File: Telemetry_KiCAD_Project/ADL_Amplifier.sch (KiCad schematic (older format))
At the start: 7 parts

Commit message: Annotated Components
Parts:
- gave numbers to parts that had none: 7
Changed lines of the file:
@@
 $Descr A4 11693 8268
 encoding utf-8
-Sheet 6 8
+Sheet 4 8
 Title ""
 Date ""
@@
 $EndDescr
 $Comp
-L power:GND #PWR?
+L power:GND #PWR0112
 U 1 1 619F7B7D
 P 4150 3300
-F 0 "#PWR?" H 4150 3050 50  0001 C CNN
+F 0 "#PWR0112" H 4150 3050 50  0001 C CNN
 F 1 "GND" H 4155 3127 50  0000 C CNN
 F 2 "" H 4150 3300 50  0001 C CNN
@@
 $EndComp
 $Comp
-L Device:L_Small L?
+L Device:L_Small L7
 U 1 1 619F8B95
 P 3500 3100
-F 0 "L?" V 3685 3100 50  0000 C CNN
+F 0 "L7" V 3685 3100 50  0000 C CNN
 F 1 "L_Small" V 3594 3100 50  0000 C CNN
 F 2 "" H 3500 3100 50  0001 C CNN
@@
 $EndComp
 $Comp
-L Device:C_Small C?
+L Device:C_Small C9
 U 1 1 619F9969
 P 3200 3250
-F 0 "C?" H 3108 3204 50  0000 R CNN
+F 0 "C9" H 3108 3204 50  0000 R CNN
 F 1 "2.4pF" H 3108 3295 50  0000 R CNN
 F 2 "" H 3200 3250 50  0001 C CNN
@@
 $EndComp
 $Comp
-L power:GND #PWR?
+L power:GND #PWR0113
 U 1 1 619F9C64
 P 3200 3350
-F 0 "#PWR?" H 3200 3100 50  0001 C CNN
+F 0 "#PWR0113" H 3200 3100 50  0001 C CNN
 F 1 "GND" H 3205 3177 50  0000 C CNN
 F 2 "" H 3200 3350 50  0001 C CNN
@@
 Connection ~ 3200 3100
 $Comp
-L RDT_Custom_Symbols:ADL5521 U?
+L RDT_Custom_Symbols:ADL5521 U3
 U 1 1 619FB6E9
 P 3850 2850
-F 0 "U?" H 4150 3015 50  0000 C CNN
+F 0 "U3" H 4150 3015 50  0000 C CNN
 F 1 "ADL5521" H 4150 2924 50  0000 C CNN
 F 2 "Package_CSP:Analog_LFCSP-8-1EP_3x3mm_P0.5mm_EP1.53x1.85mm" H 4150 3100 50  0001 C CNN
@@
 $EndComp
 $Comp
-L Device:R_Small R?
+L Device:R_Small R1
 U 1 1 619FBF87
 P 4150 2600
-F 0 "R?" V 3954 2600 50  0000 C CNN
+F 0 "R1" V 3954 2600 50  0000 C CNN
 F 1 "1.3k" V 4045 2600 50  0000 C CNN
 F 2 "" H 4150 2600 50  0001 C CNN
@@
 Connection ~ 4550 2600
 $Comp
-L Device:L_Small L?
+L Device:L_Small L8
 U 1 1 619FDCB0
 P 4550 2300
-F 0 "L?" H 4700 2250 50  0000 R CNN
+F 0 "L8" H 4700 2250 50  0000 R CNN
 F 1 "3.4nH" H 4900 2350 50  0000 R CNN
 F 2 "" H 4550 2300 50  0001 C CNN
@@
 $EndComp
 $Comp
-L Device:C_Small C?
+L Device:C_Small C10
 U 1 1 619FE8E9
 P 4750 2100
-F 0 "C?" V 4521 2100 50  0000 C CNN
+F 0 "C10" V 4521 2100 50  0000 C CNN
 F 1 "100nF" V 4600 2150 50  0000 C CNN
 F 2 "" H 4750 2100 50  0001 C CNN
@@
 	4550 2100 4650 2100
 $Comp
-L power:GND #PWR?
+L power:GND #PWR0114
 U 1 1 619FF3E9
 P 5000 2200
-F 0 "#PWR?" H 5000 1950 50  0001 C CNN
+F 0 "#PWR0114" H 5000 1950 50  0001 C CNN
 F 1 "GND" H 5005 2027 50  0000 C CNN
 F 2 "" H 5000 2200 50  0001 C CNN
@@
 	5000 2100 4850 2100
 $Comp
-L Device:R_Small R?
+L Device:R_Small R2
 U 1 1 61A005B8
 P 4550 1950
-F 0 "R?" H 4750 1900 50  0000 R CNN
+F 0 "R2" H 4750 1900 50  0000 R CNN
 F 1 "R_Small" H 4950 2000 50  0000 R CNN
 F 2 "" H 4550 1950 50  0001 C CNN
@@
 	4550 2400 4550 2600
 $Comp
-L power:+5V #PWR?
+L power:+5V #PWR0115
 U 1 1 61A03221
 P 4550 1800
-F 0 "#PWR?" H 4550 1650 50  0001 C CNN
+F 0 "#PWR0115" H 4550 1650 50  0001 C CNN
 F 1 "+5V" H 4565 1973 50  0000 C CNN
 F 2 "" H 4550 1800 50  0001 C CNN

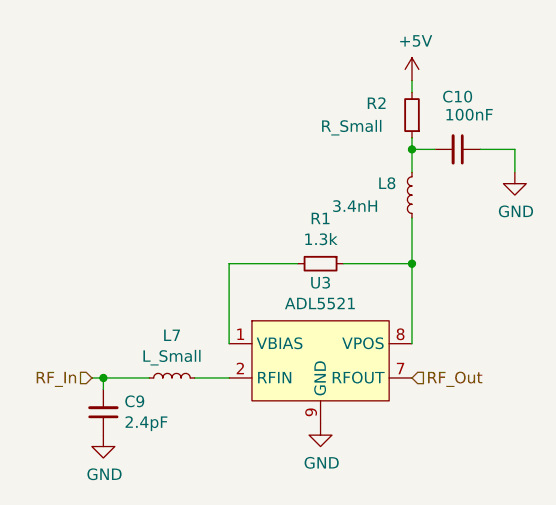
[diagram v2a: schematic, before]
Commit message: Corrected hierarchical pin directions, squashed bugs
There are still some warnings about pins being connected but not driven, don't know how to fix those at the moment
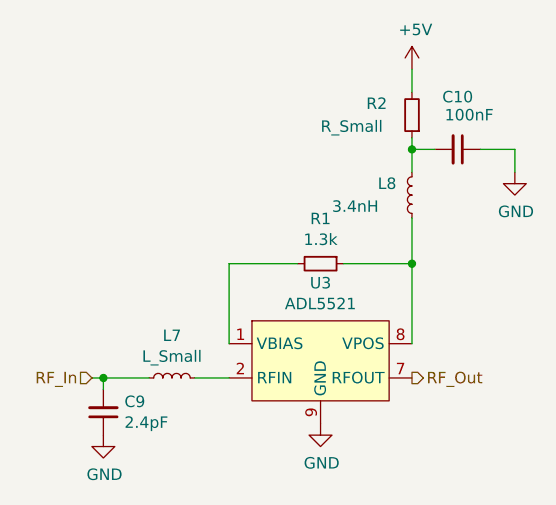
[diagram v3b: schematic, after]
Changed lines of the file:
@@
 Wire Wire Line
 	4550 2600 4550 2950
-Text HLabel 4550 3100 2    50   Input ~ 0
+Text HLabel 4550 3100 2    50   Output ~ 0
 RF_Out
 Connection ~ 4550 2600
@@
 L power:+5V #PWR0115
 U 1 1 61A03221
-P 4550 1800
-F 0 "#PWR0115" H 4550 1650 50  0001 C CNN
-F 1 "+5V" H 4565 1973 50  0000 C CNN
-F 2 "" H 4550 1800 50  0001 C CNN
-F 3 "" H 4550 1800 50  0001 C CNN
-	1    4550 1800
+P 4550 1750
+F 0 "#PWR0115" H 4550 1600 50  0001 C CNN
+F 1 "+5V" H 4565 1923 50  0000 C CNN
+F 2 "" H 4550 1750 50  0001 C CNN
+F 3 "" H 4550 1750 50  0001 C CNN
+	1    4550 1750
 	1    0    0    -1
 $EndComp
 Wire Wire Line
-	4550 1800 4550 1850
+	4550 1750 4550 1850
 $EndSCHEMATC

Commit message: Assigned footprints to all components (except duplexer)
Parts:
- C10, C9: footprint (none) -> Capacitor_SMD:C_0603_1608Metric
- L7, L8: footprint (none) -> Inductor_SMD:L_0603_1608Metric
- R1, R2: footprint (none) -> Resistor_SMD:R_0201_0603Metric
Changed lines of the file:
@@
 F 0 "L7" V 3685 3100 50  0000 C CNN
 F 1 "L_Small" V 3594 3100 50  0000 C CNN
-F 2 "" H 3500 3100 50  0001 C CNN
+F 2 "Inductor_SMD:L_0603_1608Metric" H 3500 3100 50  0001 C CNN
 F 3 "~" H 3500 3100 50  0001 C CNN
 	1    3500 3100
@@
 F 0 "C9" H 3108 3204 50  0000 R CNN
 F 1 "2.4pF" H 3108 3295 50  0000 R CNN
-F 2 "" H 3200 3250 50  0001 C CNN
+F 2 "Capacitor_SMD:C_0603_1608Metric" H 3200 3250 50  0001 C CNN
 F 3 "~" H 3200 3250 50  0001 C CNN
 	1    3200 3250
@@
 F 0 "R1" V 3954 2600 50  0000 C CNN
 F 1 "1.3k" V 4045 2600 50  0000 C CNN
-F 2 "" H 4150 2600 50  0001 C CNN
+F 2 "Resistor_SMD:R_0201_0603Metric" H 4150 2600 50  0001 C CNN
 F 3 "~" H 4150 2600 50  0001 C CNN
 	1    4150 2600
@@
 F 0 "L8" H 4700 2250 50  0000 R CNN
 F 1 "3.4nH" H 4900 2350 50  0000 R CNN
-F 2 "" H 4550 2300 50  0001 C CNN
+F 2 "Inductor_SMD:L_0603_1608Metric" H 4550 2300 50  0001 C CNN
 F 3 "~" H 4550 2300 50  0001 C CNN
 	1    4550 2300
@@
 F 0 "C10" V 4521 2100 50  0000 C CNN
 F 1 "100nF" V 4600 2150 50  0000 C CNN
-F 2 "" H 4750 2100 50  0001 C CNN
+F 2 "Capacitor_SMD:C_0603_1608Metric" H 4750 2100 50  0001 C CNN
 F 3 "~" H 4750 2100 50  0001 C CNN
 	1    4750 2100
@@
 F 0 "R2" H 4750 1900 50  0000 R CNN
 F 1 "R_Small" H 4950 2000 50  0000 R CNN
-F 2 "" H 4550 1950 50  0001 C CNN
+F 2 "Resistor_SMD:R_0201_0603Metric" H 4550 1950 50  0001 C CNN
 F 3 "~" H 4550 1950 50  0001 C CNN
 	1    4550 1950

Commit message: Created separate schematics for chips acting in TX and RX
Added link to document describing passive component selection
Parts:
- U3: footprint Package_CSP:Analog_LFCSP-8-1EP_3x3mm_P0.5mm_EP1.53x1.85mm -> Package_CSP:LFCSP-8-1EP_3x3mm_P0.5mm_EP1.45x1.74mm
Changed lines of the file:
@@
 F 0 "U3" H 4150 3015 50  0000 C CNN
 F 1 "ADL5521" H 4150 2924 50  0000 C CNN
-F 2 "Package_CSP:Analog_LFCSP-8-1EP_3x3mm_P0.5mm_EP1.53x1.85mm" H 4150 3100 50  0001 C CNN
+F 2 "Package_CSP:LFCSP-8-1EP_3x3mm_P0.5mm_EP1.45x1.74mm" H 4150 3100 50  0001 C CNN
 F 3 "https://www.analog.com/media/en/technical-documentation/data-sheets/ADL5521.pdf" H 3850 2850 50  0001 C CNN
 	1    3850 2850

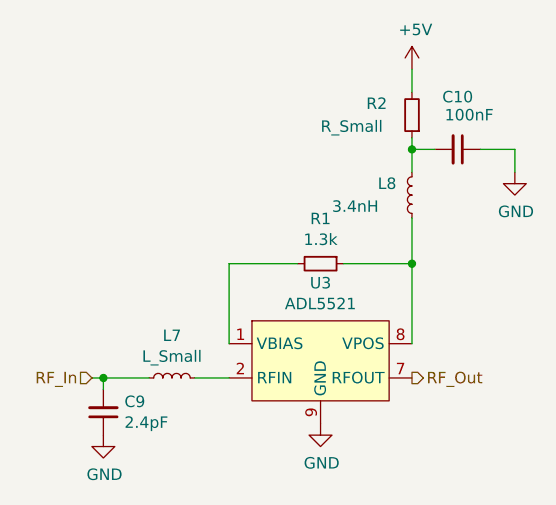
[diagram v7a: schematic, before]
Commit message: Added RSD Duplexer Footprint, rearranged RF matching networks
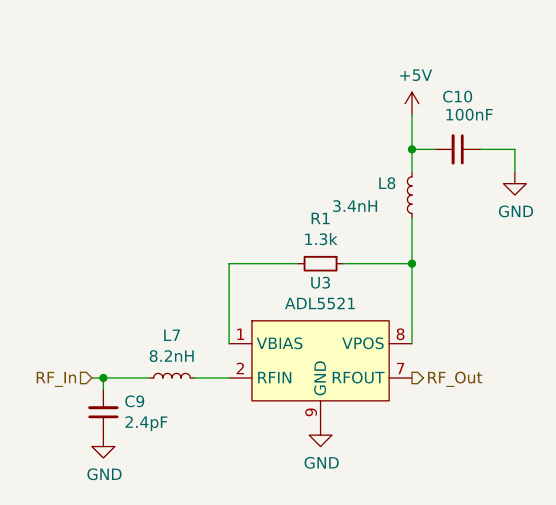
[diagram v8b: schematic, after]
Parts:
- removed R2: R_Small, Resistor_SMD:R_0201_0603Metric, symbol Device:R_Small
- L7: value L_Small -> 8.2nH
- R1: footprint Resistor_SMD:R_0201_0603Metric -> Resistors:0603
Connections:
- net +5V: now also C10.2, L8.2
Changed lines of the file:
@@
-$EndComp
-$Comp
-L Device:L_Small L7
-U 1 1 619F8B95
-P 3500 3100
-F 0 "L7" V 3685 3100 50  0000 C CNN
-F 1 "L_Small" V 3594 3100 50  0000 C CNN
-F 2 "Inductor_SMD:L_0603_1608Metric" H 3500 3100 50  0001 C CNN
-F 3 "~" H 3500 3100 50  0001 C CNN
-	1    3500 3100
-	0    -1   -1   0
 $EndComp
 $Comp
@@
 F 0 "R1" V 3954 2600 50  0000 C CNN
 F 1 "1.3k" V 4045 2600 50  0000 C CNN
-F 2 "Resistor_SMD:R_0201_0603Metric" H 4150 2600 50  0001 C CNN
+F 2 "Resistors:0603" H 4150 2600 50  0001 C CNN
 F 3 "~" H 4150 2600 50  0001 C CNN
 	1    4150 2600
@@
 Wire Wire Line
 	5000 2100 4850 2100
-$Comp
-L Device:R_Small R2
-U 1 1 61A005B8
-P 4550 1950
-F 0 "R2" H 4750 1900 50  0000 R CNN
-F 1 "R_Small" H 4950 2000 50  0000 R CNN
-F 2 "Resistor_SMD:R_0201_0603Metric" H 4550 1950 50  0001 C CNN
-F 3 "~" H 4550 1950 50  0001 C CNN
-	1    4550 1950
-	-1   0    0    1
-$EndComp
-Wire Wire Line
-	4550 2050 4550 2100
 Connection ~ 4550 2100
 Wire Wire Line
 	4550 2400 4550 2600
 $Comp
+L Device:L_Small L7
+U 1 1 619F8B95
+P 3500 3100
+F 0 "L7" V 3685 3100 50  0000 C CNN
+F 1 "8.2nH" V 3594 3100 50  0000 C CNN
+F 2 "Inductor_SMD:L_0603_1608Metric" H 3500 3100 50  0001 C CNN
+F 3 "~" H 3500 3100 50  0001 C CNN
+	1    3500 3100
+	0    -1   -1   0
+$EndComp
+$Comp
 L power:+5V #PWR0115
 U 1 1 61A03221
-P 4550 1750
-F 0 "#PWR0115" H 4550 1600 50  0001 C CNN
-F 1 "+5V" H 4565 1923 50  0000 C CNN
-F 2 "" H 4550 1750 50  0001 C CNN
-F 3 "" H 4550 1750 50  0001 C CNN
-	1    4550 1750
+P 4550 1950
+F 0 "#PWR0115" H 4550 1800 50  0001 C CNN
+F 1 "+5V" H 4565 2123 50  0000 C CNN
+F 2 "" H 4550 1950 50  0001 C CNN
+F 3 "" H 4550 1950 50  0001 C CNN
+	1    4550 1950
 	1    0    0    -1
 $EndComp
 Wire Wire Line
-	4550 1750 4550 1850
+	4550 1950 4550 2100
 $EndSCHEMATC
